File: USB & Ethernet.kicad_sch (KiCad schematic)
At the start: 22 parts

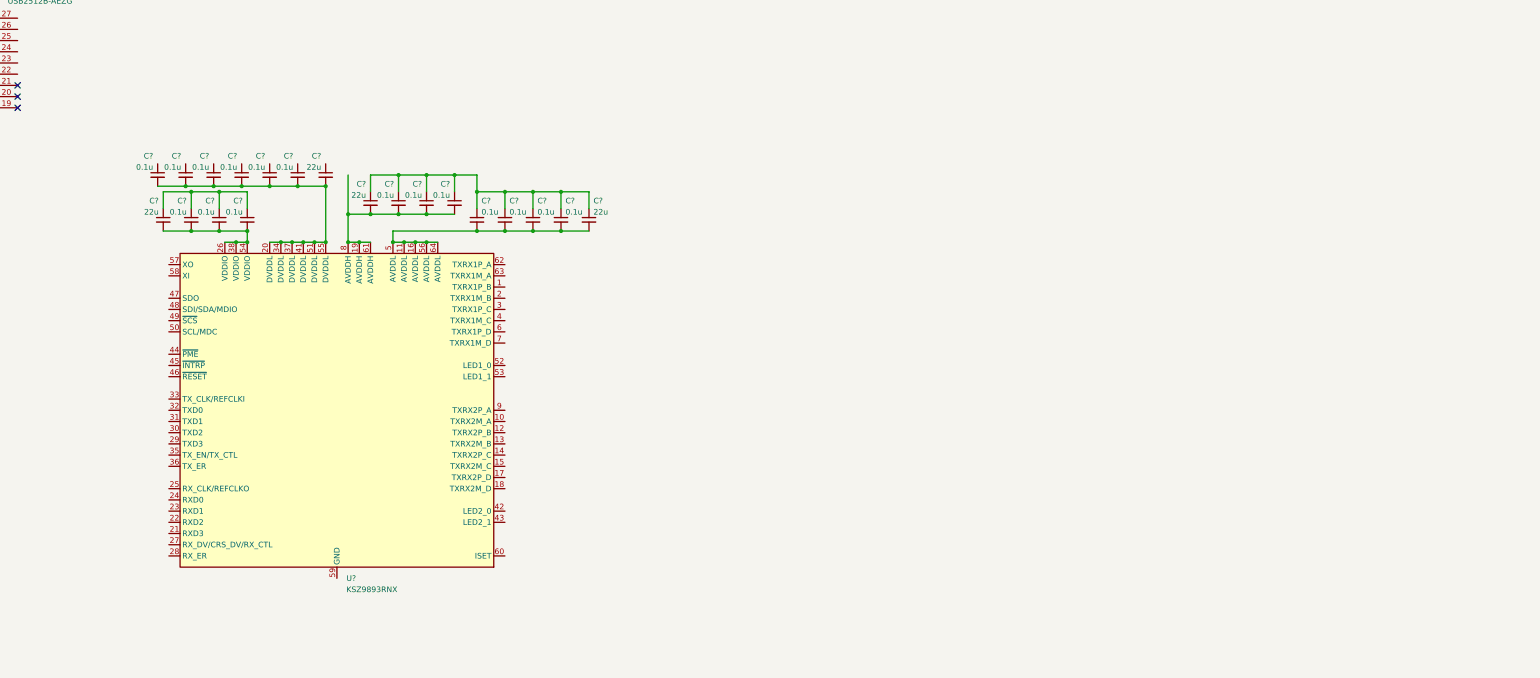
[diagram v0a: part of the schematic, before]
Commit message: Buck converter output voltage changed
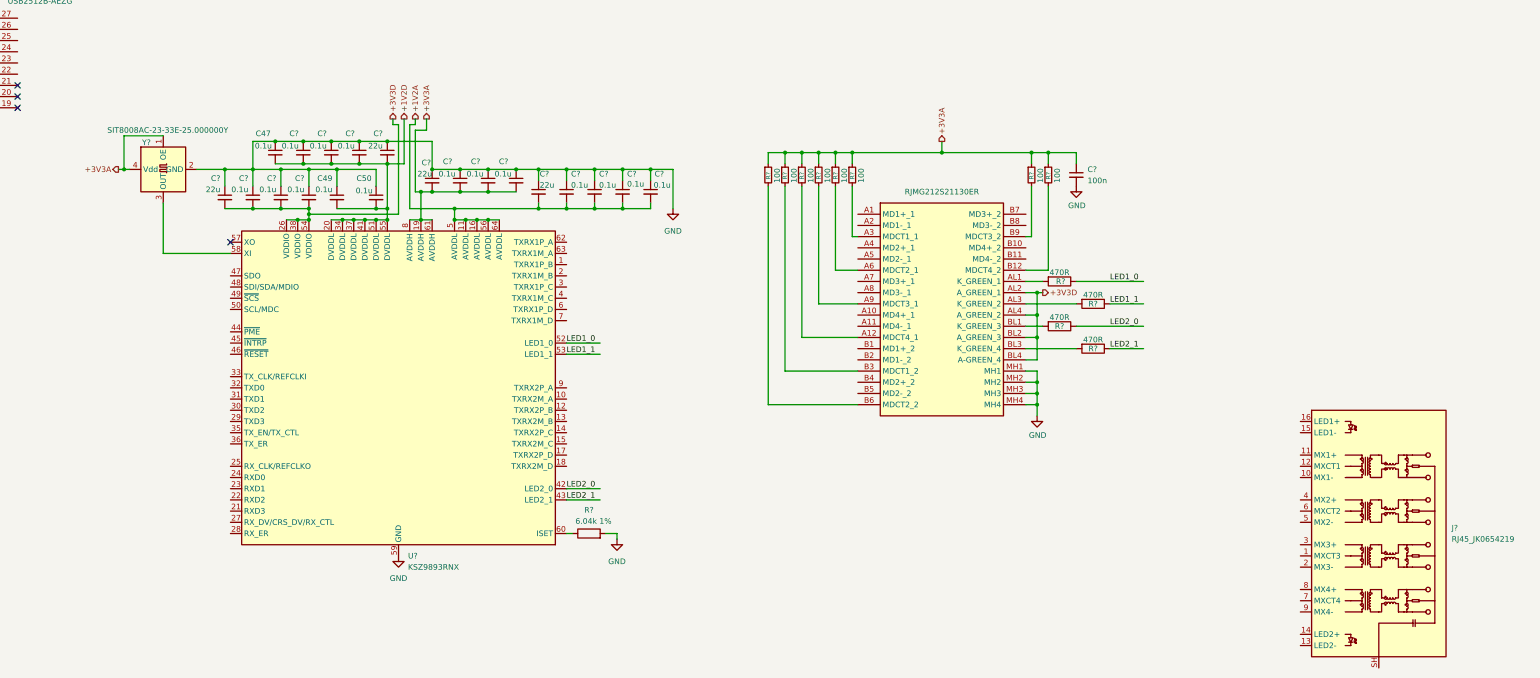
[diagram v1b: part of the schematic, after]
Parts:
- removed C? (x3): 0.1u, symbol Device:C_Small
- added C47, C49, C50: 0.1u, symbol Device:C_Small
- added C?: 100n, symbol Device:C_Small
- added J?: RJ45_JK0654219, Connector_RJ:RJ45_Pulse_JK0654219NL_Horizontal, symbol Connector:RJ45_JK0654219
- added J?: RJMG212S21130ER, RJMG212S21130ER, symbol RJMG212S21130ER:RJMG212S21130ER
- added R? (x8): 100, symbol Device:R_Small
- added R? (x4): 470R, Resistor_SMD:R_0402_1005Metric, symbol Device:R
- added R?: 6.04k 1%, symbol Device:R
- added Y?: SIT8008AC-23-33E-25.000000Y, Oscillator:Oscillator_SMD_SiT_PQFN-4Pin_3.2x2.5mm, symbol Oscillator:SiT8008xx-2x-xxE
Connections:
- net GND: now reaches C?.1, C?.1, C?.1, C?.1
- net GND: now also C?.1, C?.1, C?.1, C?.1, C?.1, C?.1, C?.1, C?.1, C?.1, C?.1, C?.1, C?.1, C?.1, U?.59 (GND), U?.65 (GND), C47.1, C49.1, C50.1, C?.2, J?.MH1, J?.MH2, J?.MH3, J?.MH4, R?.2, Y?.2 (GND)
- net +3V3D: now reaches C?.2, C?.2, C?.2, C?.2, U?.26 (VDDIO), U?.38 (VDDIO), U?.54 (VDDIO)
- net +3V3D: now also J?.AL2 (A_GREEN_1), J?.AL4 (A_GREEN_2), J?.BL2 (A_GREEN_3), J?.BL4 (A-GREEN_4)
- net +1V2A: now reaches C?.2, C?.2, C?.2, C?.2, C?.2, U?.11 (AVDDL), U?.16 (AVDDL), U?.5 (AVDDL), U?.56 (AVDDL), U?.64 (AVDDL)
- net +3V3A: now reaches C?.2, C?.2, C?.2, C?.2, U?.19 (AVDDH), U?.61 (AVDDH), U?.8 (AVDDH)
- net +3V3A: now also C?.1, R?.1, R?.1, R?.1, R?.1, R?.1, R?.1, R?.1, R?.1, Y?.1 (OE), Y?.4 (Vdd)
- net +1V2D: now reaches C?.2, C?.2, C?.2, C?.2, U?.20 (DVDDL), U?.34 (DVDDL), U?.37 (DVDDL), U?.41 (DVDDL), U?.51 (DVDDL), U?.55 (DVDDL)
- net +1V2D: now also C47.2, C49.2, C50.2
- net LED2_0: now reaches U?.42 (LED2_0)
- net LED2_0: now also R?.1
- net LED2_1: now reaches U?.43 (LED2_1)
- net LED2_1: now also R?.1
- net LED1_0: now reaches U?.52 (LED1_0)
- net LED1_0: now also R?.1
- net LED1_1: now reaches U?.53 (LED1_1)
- net LED1_1: now also R?.1
- net at U?.58 (XI): now also Y?.3 (OUT)
- net at U?.60 (ISET): now also R?.1
- new net: J?.A6 (MDCT2_1), R?.2
- new net: J?.B6 (MDCT2_2), R?.2
- new net: J?.A9 (MDCT3_1), R?.2
- new net: J?.B12 (MDCT4_2), R?.2
- new net: J?.AL1 (K_GREEN_1), R?.2
- new net: J?.AL3 (K_GREEN_2), R?.2
- new net: J?.B9 (MDCT3_2), R?.2
- new net: J?.A3 (MDCT1_1), R?.2
- new net: J?.B3 (MDCT1_2), R?.2
- new net: J?.A12 (MDCT4_1), R?.2
- new net: J?.BL1 (K_GREEN_3), R?.2
- new net: J?.BL3 (K_GREEN_4), R?.2
- no-connect marks 8 -> 9
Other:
- moved on the sheet: C?, U?

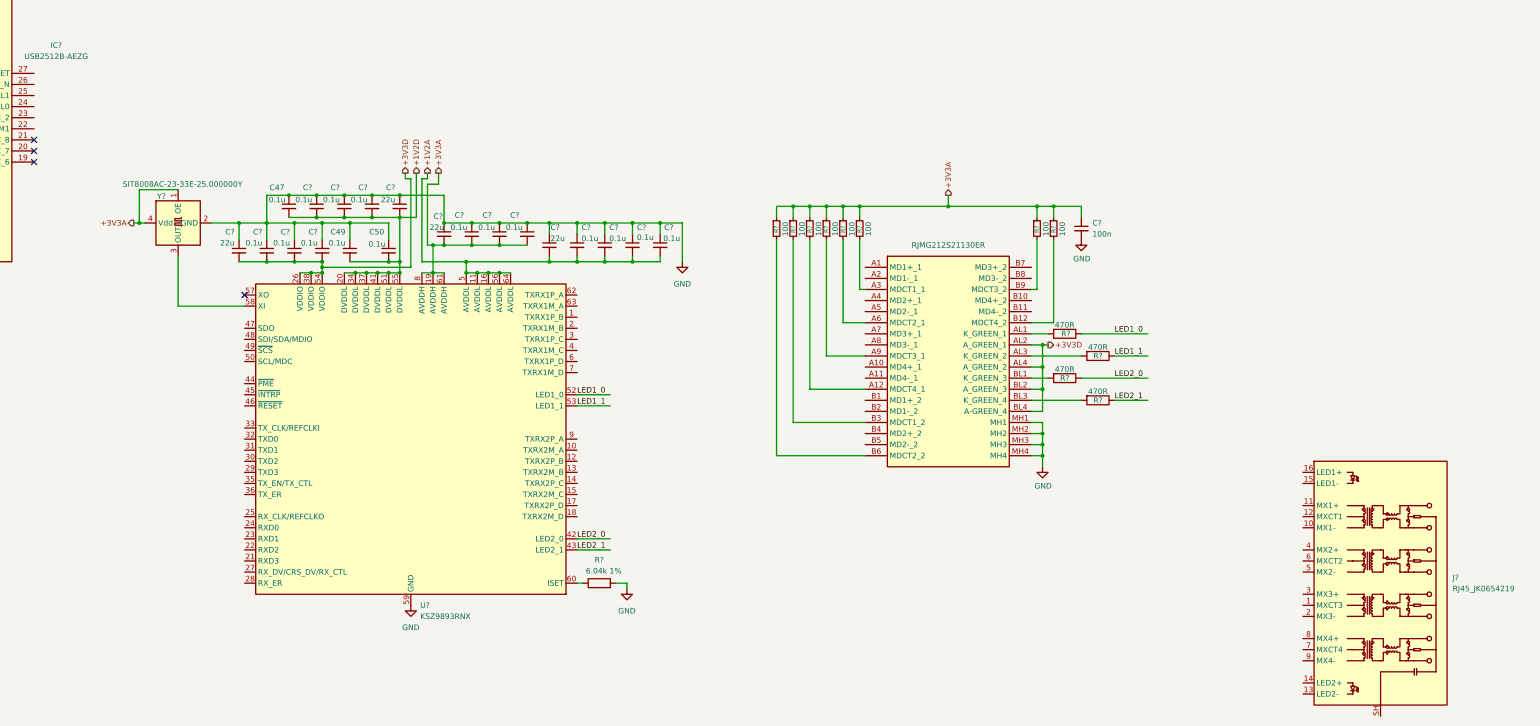
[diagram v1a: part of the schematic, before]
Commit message: etherenet schematic
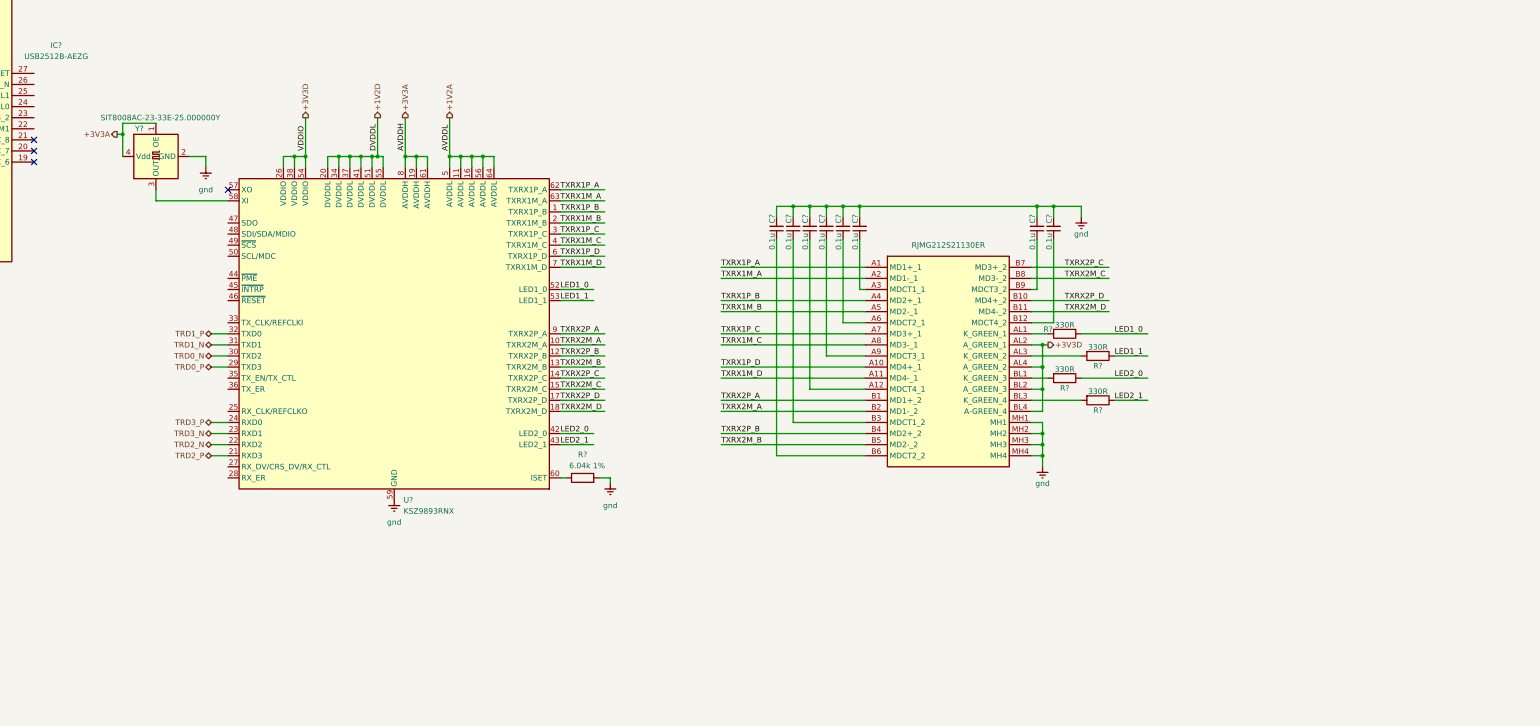
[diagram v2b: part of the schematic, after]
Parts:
- removed C47, C49, C50, C? (x13): 0.1u, symbol Device:C_Small
- removed C? (x4): 22u, symbol Device:C_Small
- removed C?: 100n, symbol Device:C_Small
- removed J?: RJ45_JK0654219, Connector_RJ:RJ45_Pulse_JK0654219NL_Horizontal, symbol Connector:RJ45_JK0654219
- removed R? (x8): 100, symbol Device:R_Small
- added C? (x8): 0.1u, symbol Device:C_Small
- R? (x4): value 470R -> 330R
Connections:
- net at J?.A6 (MDCT2_1): now also C?.1
- net at J?.B6 (MDCT2_2): now also C?.1
- net at J?.A9 (MDCT3_1): now also C?.1
- net TXRX1P_B: now reaches U?.1 (TXRX1P_B)
- net TXRX1P_B: now also J?.A4 (MD2+_1)
- net TXRX2M_A: now reaches U?.10 (TXRX2M_A)
- net TXRX2M_A: now also J?.B2 (MD1-_2)
- net TXRX2P_B: now reaches U?.12 (TXRX2P_B)
- net TXRX2P_B: now also J?.B4 (MD2+_2)
- net TXRX2M_B: now reaches U?.13 (TXRX2M_B)
- net TXRX2M_B: now also J?.B5 (MD2-_2)
- net TXRX2P_C: now reaches U?.14 (TXRX2P_C)
- net TXRX2P_C: now also J?.B7 (MD3+_2)
- net TXRX2M_C: now reaches U?.15 (TXRX2M_C)
- net TXRX2M_C: now also J?.B8 (MD3-_2)
- net TXRX2P_D: now reaches U?.17 (TXRX2P_D)
- net TXRX2P_D: now also J?.B10 (MD4+_2)
- net TXRX2M_D: now reaches U?.18 (TXRX2M_D)
- net TXRX2M_D: now also J?.B11 (MD4-_2)
- net TXRX1M_B: now reaches U?.2 (TXRX1M_B)
- net TXRX1M_B: now also J?.A5 (MD2-_1)
- net TRD2_P: now reaches U?.21 (RXD3)
- net TRD2_N: now reaches U?.22 (RXD2)
- net TRD3_N: now reaches U?.23 (RXD1)
- net TRD3_P: now reaches U?.24 (RXD0)
- net TRD0_P: now reaches U?.29 (TXD3)
- net TXRX1P_C: now reaches U?.3 (TXRX1P_C)
- net TXRX1P_C: now also J?.A7 (MD3+_1)
- net TRD0_N: now reaches U?.30 (TXD2)
- net TRD1_N: now reaches U?.31 (TXD1)
- net TRD1_P: now reaches U?.32 (TXD0)
- net TXRX1M_C: now reaches U?.4 (TXRX1M_C)
- net TXRX1M_C: now also J?.A8 (MD3-_1)
- net TXRX1P_D: now reaches U?.6 (TXRX1P_D)
- net TXRX1P_D: now also J?.A10 (MD4+_1)
- net TXRX1P_A: now reaches U?.62 (TXRX1P_A)
- net TXRX1P_A: now also J?.A1 (MD1+_1)
- net TXRX1M_A: now reaches U?.63 (TXRX1M_A)
- net TXRX1M_A: now also J?.A2 (MD1-_1)
- net TXRX1M_D: now reaches U?.7 (TXRX1M_D)
- net TXRX1M_D: now also J?.A11 (MD4-_1)
- net TXRX2P_A: now reaches U?.9 (TXRX2P_A)
- net TXRX2P_A: now also J?.B1 (MD1+_2)
- net at J?.B12 (MDCT4_2): now also C?.1
- net at J?.B9 (MDCT3_2): now also C?.1
- net at J?.A3 (MDCT1_1): now also C?.1
- net at J?.B3 (MDCT1_2): now also C?.1
- net at J?.A12 (MDCT4_1): now also C?.1
- net GND renamed gnd
- net gnd: now also C?.2, C?.2, C?.2, C?.2, C?.2, C?.2, C?.2, C?.2
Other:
- moved on the sheet: R?, U?, Y?
